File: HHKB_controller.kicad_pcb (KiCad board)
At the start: 2 copper layers, 141.5 x 36 mm, 96 parts, among them CN1 CONN_15, CN2 CONN_13, J1 USB_mini_micro_B, P1 GND, P10 CONN_1, P100 CONN_2, P11 CONN_1, P110 CONN_1, P111 CONN_1, P112 CONN_1, P113 CONN_1, P114 CONN_1, P115 CONN_1, P12 CONN_1, P130 CONN_1, P131 CONN_1, P2 D+, P3 D-, P4 VUSB, P5 PD1, P6 PD0, P7 GND, P8 CONN_3X2, P9 CONN_1, Q1 N, Q2 N, Q3 N, Q5 P, SW1 SW_PUSH, SW2 SW_DPDT, U1 ATMEGA32U4, U2 TAR5SB33, U3 NCP1402, U4 MCP73831, U5 RN42, X1 16MHz

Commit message: Final fixes for Rev.D
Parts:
- removed ? (x2), P10, P11, P12, P130, P131, P9: CONN_1, PIN_1
- removed C2: 10u, keyboard_parts:C_3216
- removed D5: LED, LED_2012_HSOL
- removed JP10, JP11, JP12: JUMPER, SOLDER_JUMPER_2
- added Q10: N, keyboard_parts:MOS_FET_SOT23-3_HSOL, F.Cu at (158.9, 112.8)
- added R26: 1K, keyboard_parts:R_1608, F.Cu at (164.4, 84.3)
- added R30: 10K, keyboard_parts:R_1608, F.Cu at (154.2, 112.7)
- added SLP3-200-100-F: Val**, keyboard_parts:SLP3-200-100-F, F.Cu at (168.4, 87.0)
- added SLP3-200-100-F: Val**, keyboard_parts:SLP3-200-100-F, F.Cu at (177.0, 87.0)
- C1: value 10u -> 4.7u
- C12: value 10u -> 68u
- C15: value 68u -> 10u; footprint keyboard_parts:C_3225 -> keyboard_parts:C_6032
- CN1: value CONN_15 -> JP; footprint HHKB_JP_HRS_DF14_15P -> keyboard_parts:HHKB_JP_HRS_DF14_15P
- CN2: value CONN_13 -> PRO2; footprint HHKB_PRO2_ZH13 -> keyboard_parts:HHKB_PRO2_ZH13
- D1: footprint LED_2012_HSOL -> keyboard_parts:LED_2012_HSOL
- D10, D4: footprint LED_TH -> keyboard_parts:LED_TH
- D3, D9: value LED -> LED_DUAL; footprint LED_2012_HSOL -> keyboard_parts:LED_3025_DUAL
- J1: footprint USB_miniB_hirose_new -> keyboard_parts:USB_miniB_hirose_new
- JP1, JP2, JP3: footprint SOLDER_JUMPER_2 -> keyboard_parts:SOLDER_JUMPER_2
- L1: footprint keyboard_parts:L_7x7MM -> keyboard_parts:L_6x6MM
- P1, P110, P111, P112, P113, P114, P115, P2, P3, P5, P7: footprint PIN_1 -> keyboard_parts:PIN_1
- P100: value CONN_2 -> LIPO
- P4: footprint PIN_1_SQUARE -> keyboard_parts:PIN_1_SQUARE
- P8: footprint AVR_ICSP_3x2 -> keyboard_parts:AVR_ICSP_3x2
- PPTC1: footprint PPTC_nano -> keyboard_parts:PPTC_nano
- R11: value 10K -> Rprog
- R13: value 470 -> 1K
- R19: footprint R_1608_NOGUIDE -> keyboard_parts:R_1608_NOGUIDE
- SW1: footprint SW_TACT_TH_HORIZ_LOW -> keyboard_parts:SW_TACT_TH_HORIZ_LOW
- SW2: footprint SW_MINI_SLIDE -> keyboard_parts:SW_MINI_SLIDE
- U3: value NCP1402 -> NCP1402SN50
- U5: footprint RN42 -> keyboard_parts:RN42
- X1: footprint HC-49_SMT -> keyboard_parts:HC-49_SMT
- moved R13 36.7 mm to (173.0, 84.3), turned to 270 degrees
- moved C12 14.9 mm to (186.2, 93.7), turned to 180 degrees
- moved R18 9.92 mm to (159.1, 108.5), turned to 0 degrees
- moved D2 8.02 mm to (185.4, 101.8), turned to 180 degrees
- moved L1 6.32 mm to (178.2, 99.8), turned to 90 degrees
- moved R25 5.91 mm to (176.6, 89.8), turned to 180 degrees
- moved U3 5.32 mm to (185.3, 98.3), turned to 90 degrees
- moved C15 4.87 mm to (178.1, 93.7), turned to 0 degrees
- moved C13 4.74 mm to (187.6, 89.0)
- moved U2 4.51 mm to (187.5, 85.8)
- moved R24 4.29 mm to (185.2, 110.6), turned to 0 degrees
- moved JP2 4.11 mm to (146.8, 101.6)
- moved R17 3.81 mm to (153.8, 108.5), turned to 0 degrees
- moved R21 3.58 mm to (165.2, 95.2), turned to 0 degrees
- moved R23 3.30 mm to (180.2, 110.6), turned to 0 degrees
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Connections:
- net LIPO_SENSE renamed ADC_LIPO
- D10 pad 2: BT_INDICATOR -> /bluetooth/LED_STS
- D9 pad 2: BT_INDICATOR -> /bluetooth/LED_STS
- J1 pad 4: (no net) -> Net-(J1-Pad4)
- R10 pad 1: Net-(D3-Pad1) -> /bluetooth/PSEL
- R10 pad 2: VUSB -> Net-(D3-Pad1)
- R13 pad 1: +3.3V -> Net-(D9-Pad3)
- R13 pad 2: Net-(D5-Pad1) -> +3.3V
- R18 pad 2: GND -> Net-(Q10-PadD)
- R25 pad 1: 5V_BOOST -> +3.3V
- SW2 pad 3: (no net) -> Net-(SW2-Pad3)
- SW2 pad 6: (no net) -> Net-(SW2-Pad6)
- U1 pad 39: (no net) -> ADC_CTRL
- U3 pad 3: (no net) -> Net-(U3-Pad3)
- U5 pad 10: (no net) -> Net-(U5-Pad10)
- U5 pad 17: (no net) -> Net-(U5-Pad17)
- U5 pad 18: (no net) -> Net-(U5-Pad18)
- U5 pad 2: (no net) -> /bluetooth/SPI_MOSI
- U5 pad 20: (no net) -> Net-(U5-Pad20)
- U5 pad 23: (no net) -> /bluetooth/SPI_SS
- U5 pad 24: (no net) -> /bluetooth/SPI_MISO
- U5 pad 30: (no net) -> Net-(U5-Pad30)
- U5 pad 31: (no net) -> /bluetooth/LED_ACT
- U5 pad 32: (no net) -> Net-(U5-Pad32)
- U5 pad 33: (no net) -> Net-(U5-Pad33)
- U5 pad 34: (no net) -> Net-(U5-Pad34)
- U5 pad 35: (no net) -> Net-(U5-Pad35)
- U5 pad 4: (no net) -> Net-(U5-Pad4)
- U5 pad 5: (no net) -> /bluetooth/RN42_RST
- U5 pad 6: (no net) -> /bluetooth/SPI_SCK
- U5 pad 7: (no net) -> Net-(U5-Pad7)
- U5 pad 8: (no net) -> Net-(U5-Pad8)
- U5 pad 9: (no net) -> Net-(U5-Pad9)
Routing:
- net GND: track 440.8 -> 478.9 mm, vias 57 -> 67
- net ADC_CTRL: track 0.00 -> 28.0 mm, vias 0 -> 2
- net 5V_BOOST: track 276.3 -> 249.7 mm
- net /bluetooth/LED_STS: track 25.8 -> 48.4 mm, vias 2 -> 1
- net +3.3V: track 115.2 -> 134.5 mm, vias 1 -> 3
- net Net-(D5-Pad1): track 8.80 -> 0.00 mm
- net /bluetooth/LIPO_RAW: track 85.9 -> 78.7 mm, vias 3 -> 2
- net ADC_LIPO: track 22.4 -> 29.5 mm
- net Net-(Q10-PadD): track 0.00 -> 6.47 mm
- net /bluetooth/PSEL: track 16.1 -> 20.8 mm
- net /bluetooth/LIPO_SW: track 35.8 -> 40.4 mm, vias 1 -> 0
- net Net-(D10-Pad1): track 8.53 -> 4.77 mm
- net VUSB: track 84.0 -> 87.0 mm
- net Net-(D9-Pad3): track 0.00 -> 2.66 mm
- net Net-(D3-Pad3): track 0.00 -> 2.66 mm
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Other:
- net class Power: trace_width 0.381 -> 0.4
- board text added: "2014/09"
- board text added: "Rev.D"
- board text removed: "-"
- board text removed: "2014/07"
- board text removed: "CTS3"
- board text removed: "CTS5"
- board text removed: "RTS3"
- board text removed: "RTS5"
- board text removed: "RX3"
- board text removed: "RX5"
- board text removed: "Rev.C"
- board text removed: "TX3"
- board text removed: "TX5"
- board text removed: "amp"

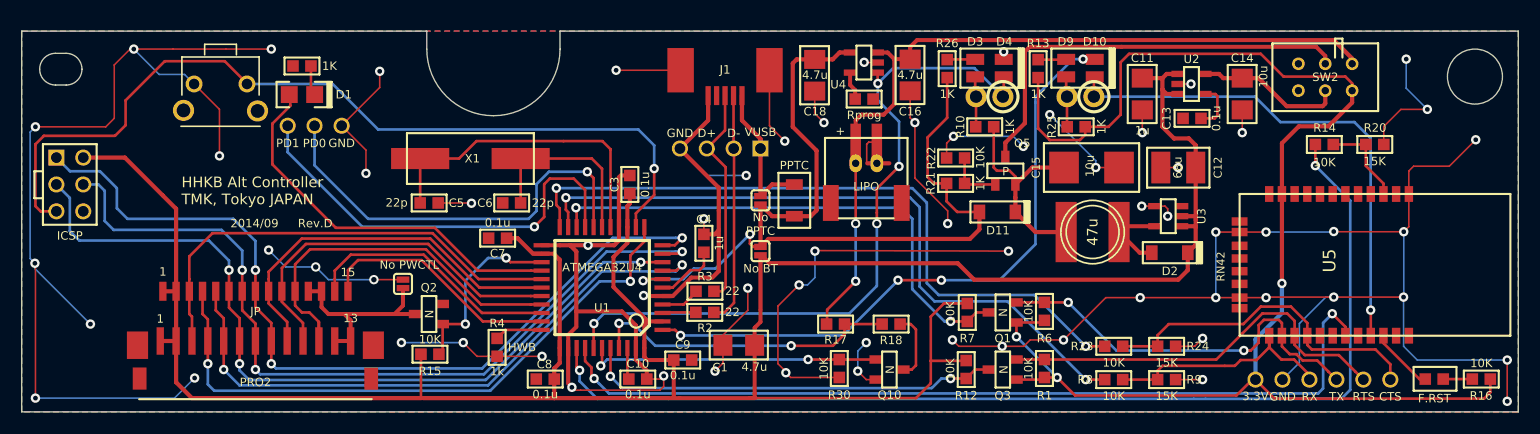
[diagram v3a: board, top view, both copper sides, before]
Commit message: Add D5 schottky and change C15 size and C14 value
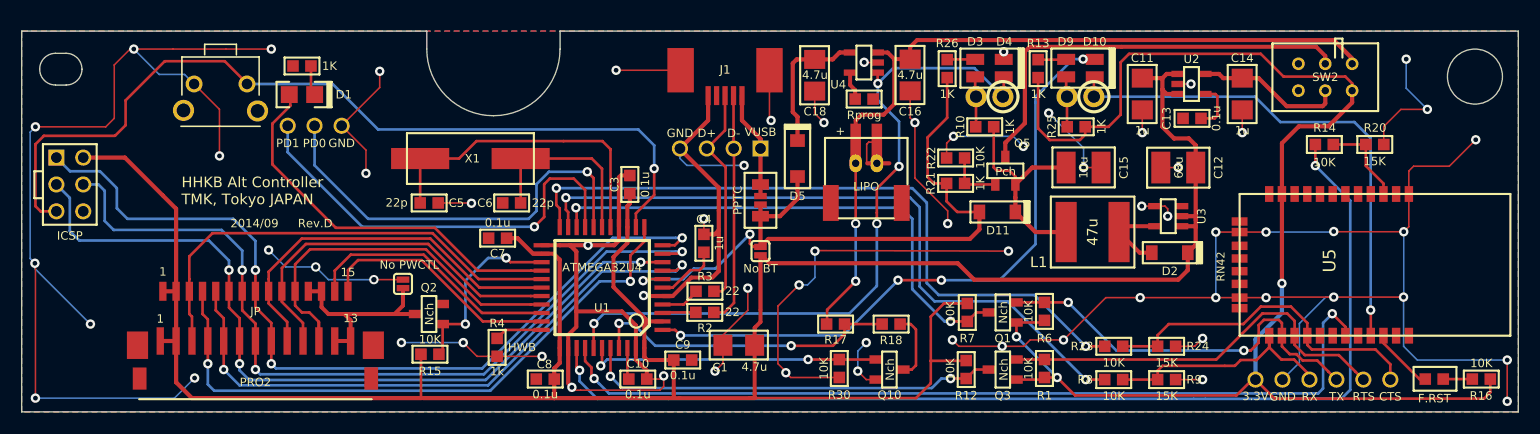
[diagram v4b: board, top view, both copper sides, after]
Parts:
- added D5: Schottky diode, keyboard_parts:D_SOD123, F.Cu at (150.2, 92.8)
- C12: footprint keyboard_parts:C_3228 -> keyboard_parts:C_3528
- C14: value 10u -> 1u
- C15: footprint keyboard_parts:C_6032 -> keyboard_parts:C_3528
- Q1, Q10, Q2, Q3: value N -> Nch
- Q5: value P -> Pch
- U2: value TAR5SB33 -> MIC5504-3.3YMTR
- moved PPTC1 3.20 mm to (146.8, 96.8)
- moved C15 0.75 mm to (177.3, 93.7)
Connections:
- C18 pad 1: VUSB -> Net-(C18-Pad1)
- U4 pad 4: VUSB -> Net-(C18-Pad1)
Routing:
- net VUSB: track 87.0 -> 66.6 mm
- net Net-(C18-Pad1): track 0.00 -> 13.3 mm
- net /VUSB_RAW: track 13.9 -> 10.2 mm
- net GND: track 478.9 -> 475.5 mm
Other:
- board text removed: "No PPTC"

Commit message: Fix ADC switch and light pipe hole size
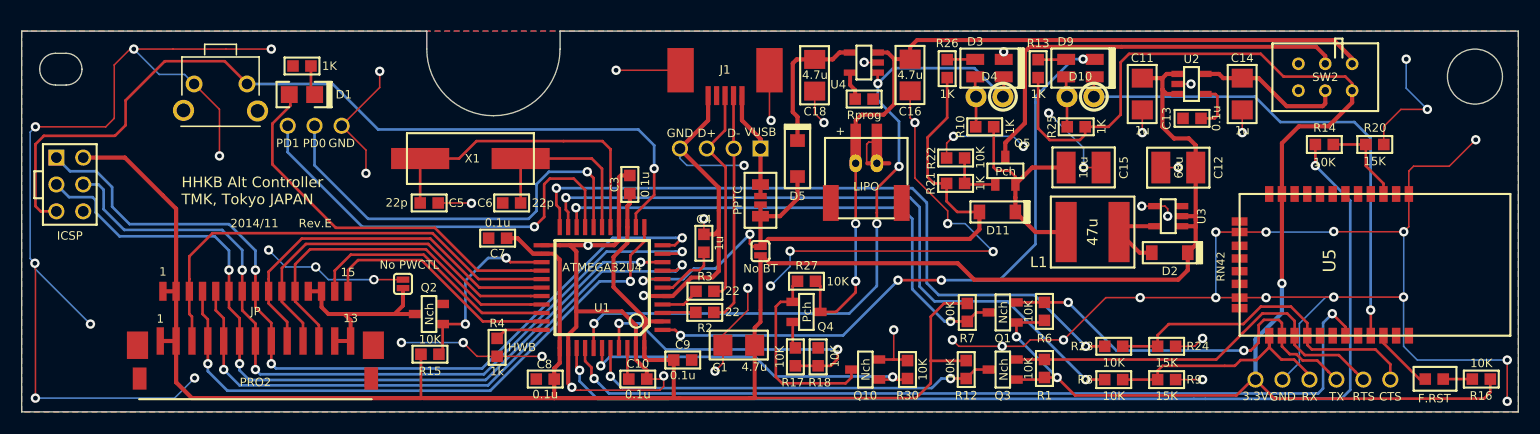
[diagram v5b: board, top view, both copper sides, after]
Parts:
- added Q4: Pch, keyboard_parts:MOS_FET_SOT23-3_HSOL, F.Cu at (151.1, 107.3)
- added R27: 10K, keyboard_parts:R_1608, F.Cu at (151.1, 104.5)
- D10, D4: footprint keyboard_parts:LED_TH -> keyboard_parts:LED_TH_BIVAR
- R17, R18: value R -> 10K
- moved R18 7.56 mm to (152.2, 111.6), turned to 90 degrees
- moved R30 6.45 mm to (160.7, 112.8), turned to 90 degrees
- moved R17 4.90 mm to (150.1, 111.6), turned to 270 degrees
- moved Q10 2.30 mm to (156.7, 112.8), turned to 90 degrees
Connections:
- R17 pad 1: /bluetooth/LIPO_RAW -> Net-(Q4-PadS)
- R18 pad 2: Net-(Q10-PadD) -> GND
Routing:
- net Net-(Q10-PadD): track 6.47 -> 18.9 mm
- net GND: track 475.5 -> 467.4 mm, vias 67 -> 65
- net ADC_CTRL: track 28.0 -> 33.5 mm
- net /bluetooth/LIPO_RAW: track 78.7 -> 81.8 mm
- net Net-(Q4-PadS): track 0.00 -> 2.55 mm
- net /PB6: track 36.4 -> 34.2 mm
- net /PB7: track 59.2 -> 58.4 mm
- net /PB1: track 76.9 -> 76.3 mm
- net /PB2: track 78.3 -> 77.8 mm
- net /PB3: track 81.8 -> 81.2 mm
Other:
- board text added: "2014/11"
- board text added: "Rev.E"
- board text removed: "2014/09"
- board text removed: "Rev.D"

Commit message: Fix UVCC
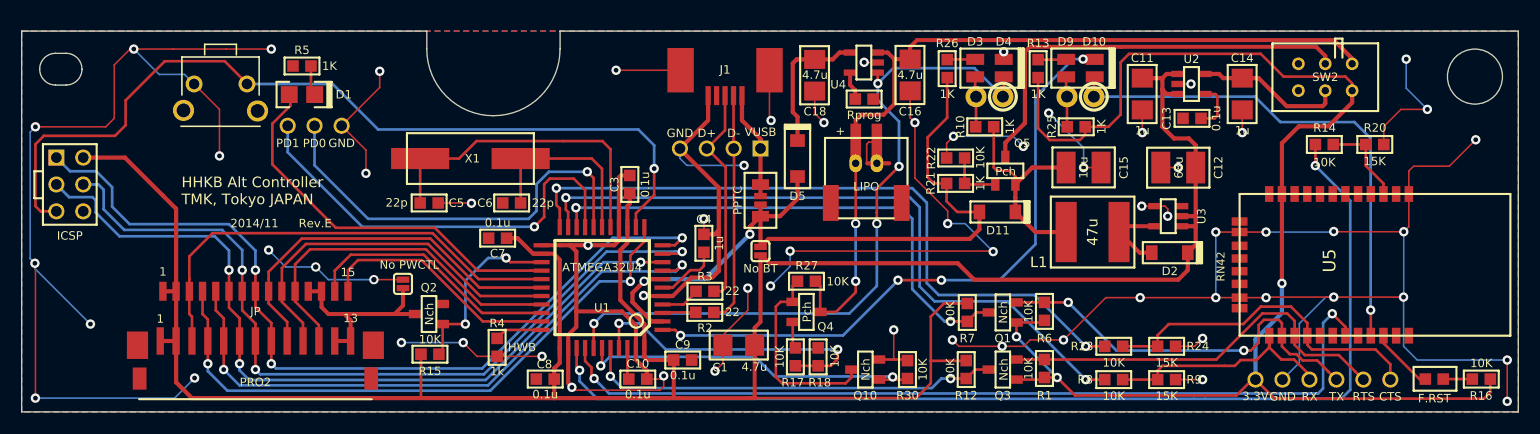
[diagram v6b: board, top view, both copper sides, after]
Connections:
- U1 pad 2: 5V_BOOST -> VUSB
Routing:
- net VUSB: track 66.6 -> 72.5 mm
- net 5V_BOOST: track 249.7 -> 246.7 mm

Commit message: Final plot of Rev.E to order PCB
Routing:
- net GND: track 467.4 -> 471.6 mm, vias 65 -> 66
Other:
- rule pad_to_mask_clearance: 0 -> 0.13
